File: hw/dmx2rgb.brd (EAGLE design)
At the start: 100 x 80 mm, 61 parts, among them IC1 ATMEGA88-20A, IC2 7805

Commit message: all parts added some parts placed
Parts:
- removed R10, R11, R12, R13, R9: 10k, dmx2rgb:CHIP_0805
- added C11, C12: 100n, dmx2rgb:CHIP_0805
- added LED1, LED2, LED3: (no value), dmx2rgb:CHIPLED_0805
- added PAD100, PAD17, PAD18, PAD19, PAD20, PAD21, PAD22, PAD23, PAD24, PAD25, PAD26, PAD27, PAD28, PAD29, PAD30, PAD31, PAD32, PAD33, PAD34, PAD35, PAD36, PAD37, PAD38, PAD39, PAD40, PAD41, PAD42, PAD43, PAD44, PAD45, PAD46, PAD47, PAD48, PAD49, PAD50, PAD51, PAD52, PAD53, PAD54, PAD55, PAD56, PAD57, PAD58, PAD59, PAD60, PAD61, PAD62, PAD63, PAD64, PAD65, PAD66, PAD67, PAD68, PAD69, PAD70, PAD71, PAD72, PAD73, PAD74, PAD75, PAD76, PAD77, PAD78, PAD79, PAD80, PAD81, PAD82, PAD83, PAD84, PAD85, PAD86, PAD87, PAD88, PAD89, PAD90, PAD91, PAD92, PAD93, PAD94, PAD95, PAD96, PAD99: (no value), dmx2rgb:SMD_PAD_LONG
- added PAD97, PAD98: (no value), dmx2rgb:SMD2,54-5,08
- added U$11, U$13, U$14, U$15, U$16, U$17, U$18, U$19, U$20, U$22, U$23, U$24, U$25, U$26, U$27, U$28: IRF7303, dmx2rgb:SO8
- added U$12, U$21: PCA9685, dmx2rgb:TSSOP28
- PAD1, PAD10, PAD11, PAD12, PAD13, PAD14, PAD15, PAD16, PAD2, PAD3, PAD4, PAD5, PAD6, PAD7, PAD8, PAD9: device dmx2rgb:PAD_THT_1.6 -> dmx2rgb:SMD_PAD_LONG
- R6, R7, R8: value 10k -> (none)
- moved SJ8 275.5 mm to (31.8, 77.5)
- moved SJ7 271.9 mm to (35.6, 77.5)
- moved SJ6 268.4 mm to (39.4, 77.5)
- moved SJ5 265.1 mm to (43.2, 77.5)
- moved SJ4 261.8 mm to (47.0, 77.5)
- moved SJ3 254.8 mm to (47.0, 74.9)
- moved SJ2 248.1 mm to (41.9, 74.9)
- moved SJ1 241.5 mm to (36.8, 74.9)
- moved R6 239.2 mm to (10.2, 43.2)
- moved R7 236.7 mm to (10.2, 38.1)
- moved R4 234.1 mm to (55.9, 64.8)
- moved R8 233.9 mm to (8.89, 33.0)
- moved C9 209.5 mm to (27.9, 69.8)
- moved C8 205.6 mm to (21.6, 72.4)
- moved C10 205.2 mm to (12.7, 63.5)
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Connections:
- removed net N$12: U$3.6
- removed net N$62: SJ5.1
- new net LED_ENABLE: IC1.1, R5.1, U$12.23, U$2.23, U$21.23
- new net N$100: PAD35.P$1, U$22.7, U$22.8
- new net N$101: PAD36.P$1, U$22.5, U$22.6
- new net N$102: U$21.10, U$22.4
- new net N$103: PAD37.P$1, U$23.7, U$23.8
- new net N$104: PAD38.P$1, U$23.5, U$23.6
- new net N$105: U$21.9, U$23.2
- new net N$106: U$21.8, U$23.4
- new net N$107: PAD39.P$1, U$24.7, U$24.8
- new net N$108: PAD40.P$1, U$24.5, U$24.6
- new net N$109: U$21.7, U$24.2
- new net N$110: U$21.6, U$24.4
- new net N$111: PAD41.P$1, U$25.7, U$25.8
- new net N$112: PAD42.P$1, U$25.5, U$25.6
- new net N$113: PAD43.P$1, U$26.7, U$26.8
- new net N$114: PAD44.P$1, U$26.5, U$26.6
- new net N$115: PAD45.P$1, U$27.7, U$27.8
- new net N$116: PAD46.P$1, U$27.5, U$27.6
- new net N$117: PAD47.P$1, U$28.7, U$28.8
- new net N$118: PAD48.P$1, U$28.5, U$28.6
- new net N$119: U$20.2, U$21.13
- new net N$120: U$20.4, U$21.12
- new net N$121: U$21.11, U$22.2
- new net N$122: U$21.15, U$25.2
- new net N$123: U$21.16, U$25.4
- new net N$124: U$21.17, U$26.2
- new net N$125: U$21.18, U$26.4
- new net N$126: U$21.19, U$27.2
- new net N$127: U$21.20, U$27.4
- new net N$128: U$21.21, U$28.2
- new net N$129: U$21.22, U$28.4
- new net N$47: PAD100.P$1, U$3.6
- new net N$48: PAD17.P$1, U$11.7, U$11.8
- new net N$49: PAD18.P$1, U$11.5, U$11.6
- new net N$61: PAD19.P$1, U$13.7, U$13.8
- new net N$63: PAD20.P$1, U$13.5, U$13.6
- new net N$64: U$12.10, U$13.4
- new net N$65: PAD21.P$1, U$14.7, U$14.8
- new net N$66: PAD22.P$1, U$14.5, U$14.6
- new net N$67: U$12.9, U$14.2
- new net N$68: U$12.8, U$14.4
- new net N$69: PAD23.P$1, U$15.7, U$15.8
- new net N$70: PAD24.P$1, U$15.5, U$15.6
- new net N$71: U$12.7, U$15.2
- new net N$72: U$12.6, U$15.4
- new net N$73: PAD25.P$1, U$16.7, U$16.8
- new net N$74: PAD26.P$1, U$16.5, U$16.6
- new net N$75: PAD27.P$1, U$17.7, U$17.8
- new net N$76: PAD28.P$1, U$17.5, U$17.6
- new net N$77: PAD29.P$1, U$18.7, U$18.8
- new net N$78: PAD30.P$1, U$18.5, U$18.6
- new net N$79: PAD31.P$1, U$19.7, U$19.8
- new net N$80: PAD32.P$1, U$19.5, U$19.6
- new net N$81: U$11.2, U$12.13
- new net N$82: U$11.4, U$12.12
- new net N$83: U$12.11, U$13.2
- new net N$84: U$12.15, U$16.2
- new net N$85: U$12.16, U$16.4
- new net N$86: U$12.17, U$17.2
- new net N$87: U$12.18, U$17.4
- new net N$88: U$12.19, U$18.2
- new net N$89: U$12.20, U$18.4
- new net N$90: U$12.21, U$19.2
- new net N$91: U$12.22, U$19.4
- new net N$98: PAD33.P$1, U$20.7, U$20.8
- new net N$99: PAD34.P$1, U$20.5, U$20.6
- net +12V: now also PAD49.P$1, PAD50.P$1, PAD51.P$1, PAD52.P$1, PAD53.P$1, PAD54.P$1, PAD55.P$1, PAD56.P$1, PAD57.P$1, PAD58.P$1, PAD59.P$1, PAD60.P$1, PAD61.P$1, PAD62.P$1, PAD63.P$1, PAD64.P$1, PAD65.P$1, PAD66.P$1, PAD67.P$1, PAD68.P$1, PAD69.P$1, PAD70.P$1, PAD71.P$1, PAD72.P$1, PAD73.P$1, PAD74.P$1, PAD75.P$1, PAD76.P$1, PAD77.P$1, PAD78.P$1, PAD79.P$1, PAD80.P$1, PAD81.P$1, PAD82.P$1, PAD83.P$1, PAD84.P$1, PAD85.P$1, PAD86.P$1, PAD87.P$1, PAD88.P$1, PAD89.P$1, PAD90.P$1, PAD91.P$1, PAD92.P$1, PAD93.P$1, PAD94.P$1, PAD95.P$1, PAD96.P$1, PAD97.1
- net +5V: now also C11.2, C12.2, LED1.A, LED2.A, LED3.A, U$12.1, U$12.2, U$12.28, U$2.1, U$21.1, U$21.2, U$21.28, U$21.3; no longer R10.2, R11.2, R12.2, R13.2, R6.2, R7.2, R8.2, R9.2
- net GND: now also C11.1, C12.1, PAD98.1, U$11.1, U$11.3, U$12.14, U$12.24, U$12.25, U$12.3, U$12.4, U$12.5, U$13.1, U$13.3, U$14.1, U$14.3, U$15.1, U$15.3, U$16.1, U$16.3, U$17.1, U$17.3, U$18.1, U$18.3, U$19.1, U$19.3, U$2.2, U$2.3, U$2.4, U$2.5, U$20.1, U$20.3, U$21.14, U$21.24, U$21.25, U$21.4, U$21.5, U$22.1, U$22.3, U$23.1, U$23.3, U$24.1, U$24.3, U$25.1, U$25.3, U$26.1, U$26.3, U$27.1, U$27.3, U$28.1, U$28.3
- net N$11: now also PAD99.P$1
- net N$15: now also LED2.C, R7.2; no longer U$2.1
- net N$27: now also LED1.C, R6.2; no longer U$2.2
- net N$28: now also IC1.12, R6.1; no longer U$2.3
- net N$3: now also LED3.C, R8.2; no longer IC1.32, R5.1, U$3.2
- net N$31: now also IC1.13, R7.1; no longer U$2.4
- net N$32: now also IC1.14, R8.1; no longer U$2.5
- net N$35: no longer R6.1
- net N$36: no longer R7.1
- net N$39: no longer R8.1
- net N$4: now also IC1.32, U$3.2; no longer IC1.1
- net N$40: no longer R9.1
- net N$43: now also IC1.2, SJ5.1; no longer IC1.11, R13.1
- net N$44: now also IC1.9; no longer IC1.12, R12.1
- net N$45: now also IC1.10; no longer IC1.13, R11.1
- net N$46: now also IC1.11; no longer IC1.14, R10.1
- net SCL: now also U$12.26, U$21.26
- net SDA: now also U$12.27, U$21.27

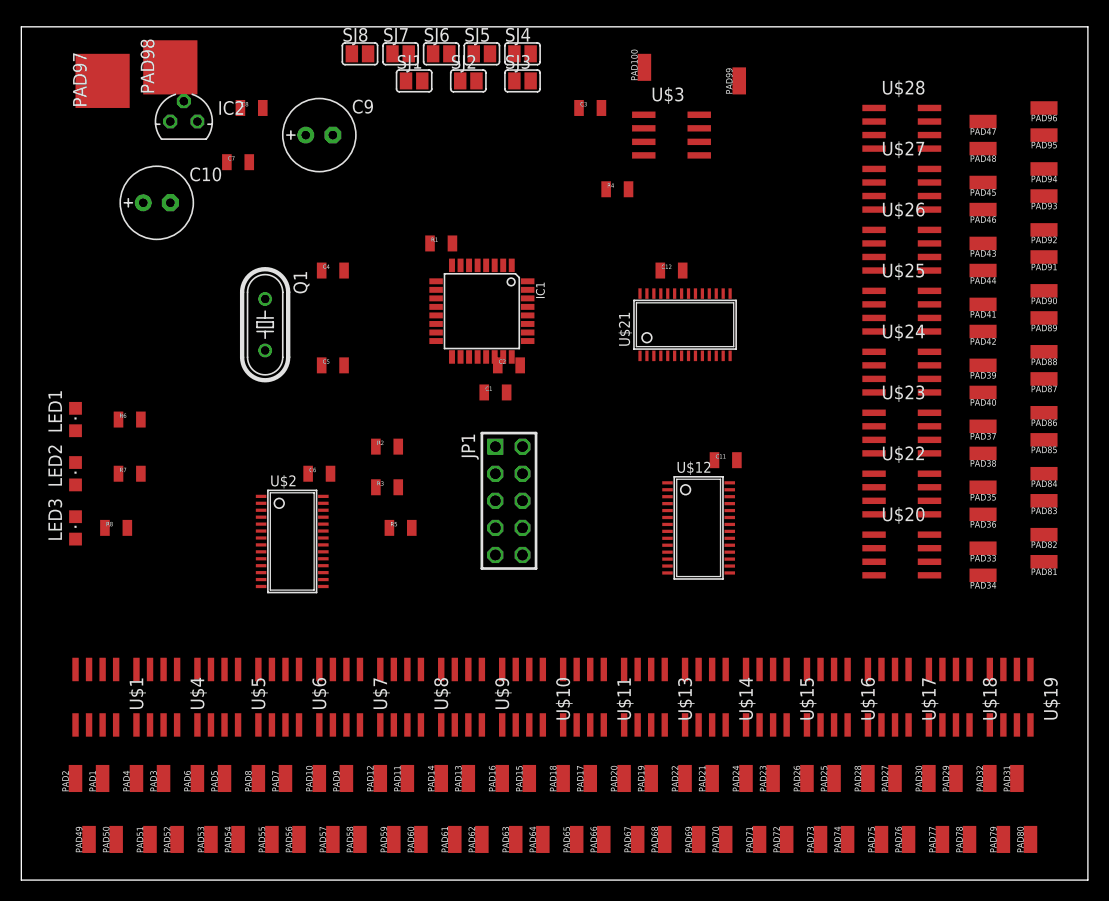
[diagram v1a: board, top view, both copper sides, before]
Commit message: pcb finished prepared for 0.3mm milling
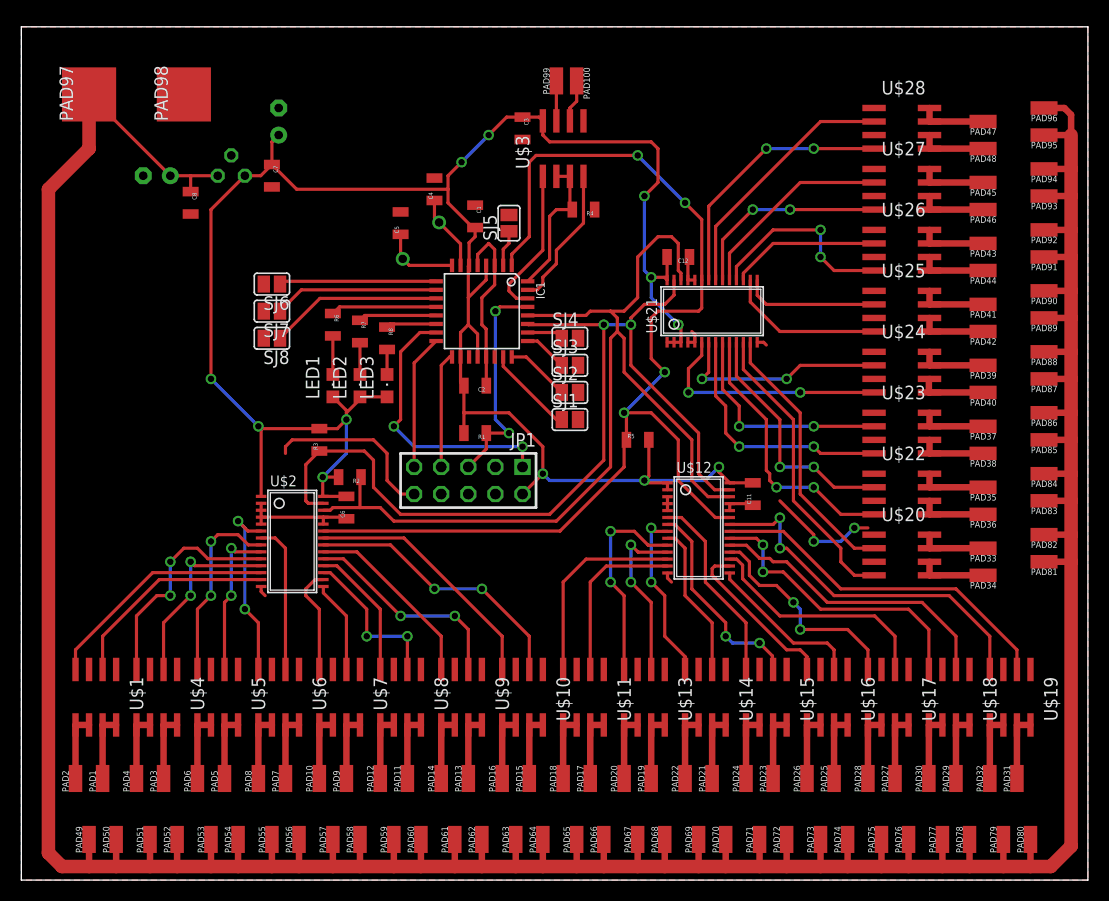
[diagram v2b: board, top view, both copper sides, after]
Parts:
- moved SJ1 34.9 mm to (51.4, 43.2)
- moved LED3 32.1 mm to (34.3, 46.4)
- moved R8 31.0 mm to (34.3, 50.8), turned to 270 degrees
- moved SJ2 30.7 mm to (51.4, 45.7)
- moved LED2 27.9 mm to (31.8, 46.4)
- moved SJ8 27.9 mm to (23.5, 50.8), turned to 180 degrees
- moved SJ3 27.0 mm to (51.4, 48.3)
- moved SJ4 27.0 mm to (51.4, 50.8)
- moved SJ7 27.0 mm to (23.5, 53.3), turned to 180 degrees
- moved SJ6 26.8 mm to (23.5, 55.9), turned to 180 degrees
- moved R7 25.4 mm to (31.8, 51.4), turned to 270 degrees
- moved LED1 24.3 mm to (29.2, 46.4)
- moved R5 23.7 mm to (57.8, 41.3)
- moved R6 21.0 mm to (29.2, 52.1), turned to 270 degrees
- moved R1 18.1 mm to (42.5, 41.9), turned to 180 degrees
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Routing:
- net +12V: track 0.00 -> 377.4 mm
- net +5V: track 0.00 -> 209.4 mm, vias 0 -> 12
- net LED_ENABLE: track 0.00 -> 105.9 mm, vias 0 -> 4
- net SCL: track 0.00 -> 91.9 mm
- net SDA: track 0.00 -> 89.7 mm, vias 0 -> 2
- net GND: track 0.00 -> 66.5 mm, vias 0 -> 2
- net N$91: track 0.00 -> 34.0 mm, vias 0 -> 2
- net N$90: track 0.00 -> 33.4 mm
- net N$120: track 0.00 -> 28.0 mm
- net N$88: track 0.00 -> 27.9 mm
- net N$89: track 0.00 -> 27.5 mm, vias 0 -> 2
- net N$8: track 0.00 -> 26.1 mm, vias 0 -> 2
- net N$59: track 0.00 -> 26.0 mm, vias 0 -> 2
- net N$102: track 0.00 -> 25.6 mm, vias 0 -> 2
- net N$119: track 0.00 -> 25.2 mm
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- added copper zone on layer 1, net GND

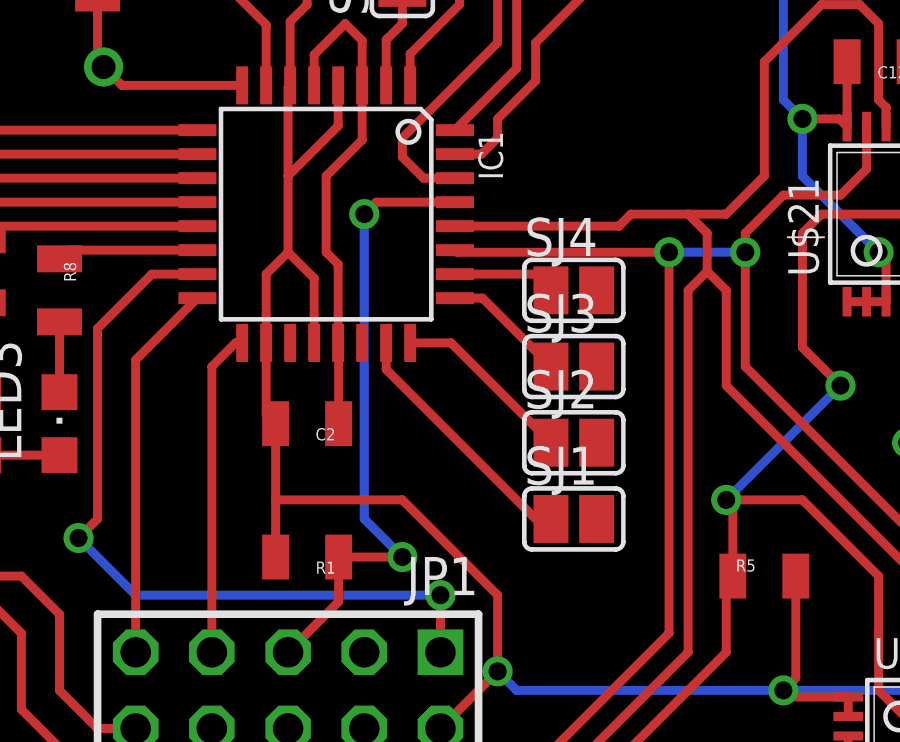
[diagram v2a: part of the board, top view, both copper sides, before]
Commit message: removed drilling below mcu
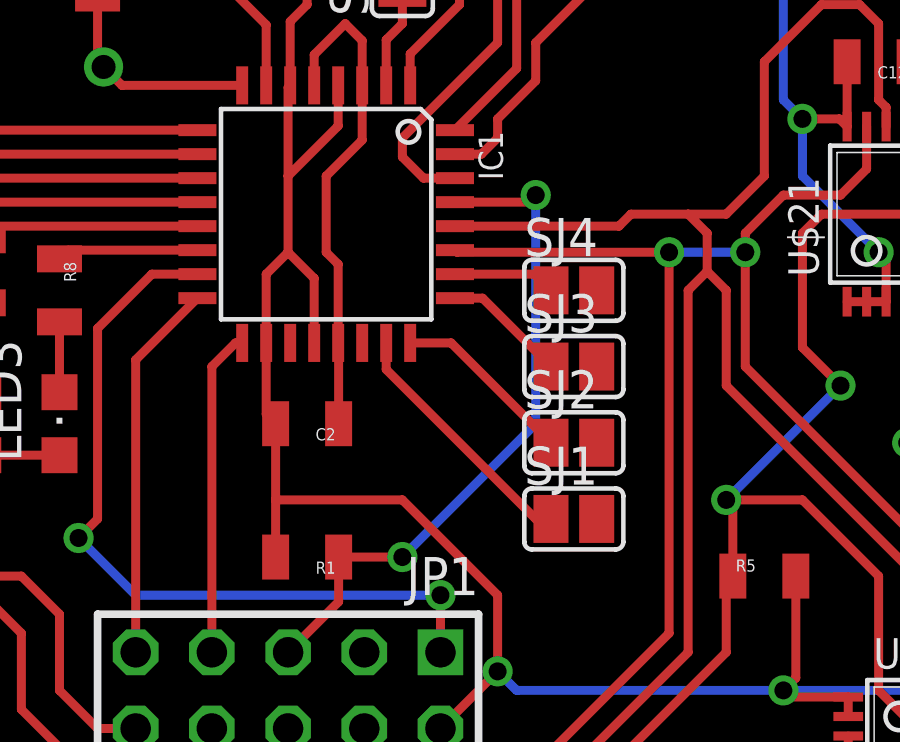
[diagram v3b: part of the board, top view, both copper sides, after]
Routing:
- net N$7: track 21.1 -> 22.7 mm
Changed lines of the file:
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@@
 <wire x1="41.91" y1="38.735" x2="43.595" y2="40.42" width="0.3" layer="1"/>
 <via x="45.72" y="41.91" extent="1-16" drill="0.6"/>
-<wire x1="44.45" y1="43.18" x2="44.45" y2="53.34" width="0.3" layer="16"/>
-<via x="44.45" y="53.34" extent="1-16" drill="0.6"/>
-<wire x1="44.45" y1="53.34" x2="44.85" y2="53.74" width="0.3" layer="1"/>
-<wire x1="44.85" y1="53.74" x2="47.4726" y2="53.74" width="0.3" layer="1"/>
+<via x="50.165" y="53.975" extent="1-16" drill="0.6"/>
 <wire x1="43.595" y1="40.42" x2="43.595" y2="41.91" width="0.3" layer="1"/>
-<wire x1="44.45" y1="43.18" x2="45.72" y2="41.91" width="0.3" layer="16"/>
 <wire x1="45.72" y1="41.91" x2="43.595" y2="41.91" width="0.3" layer="1"/>
+<wire x1="45.72" y1="41.91" x2="50.165" y2="46.355" width="0.3" layer="16"/>
+<wire x1="50.165" y1="46.355" x2="50.165" y2="53.975" width="0.3" layer="16"/>
+<wire x1="50.165" y1="53.975" x2="49.93" y2="53.74" width="0.3" layer="1"/>
+<wire x1="49.93" y1="53.74" x2="47.4726" y2="53.74" width="0.3" layer="1"/>
 </signal>
 <signal name="N$8">

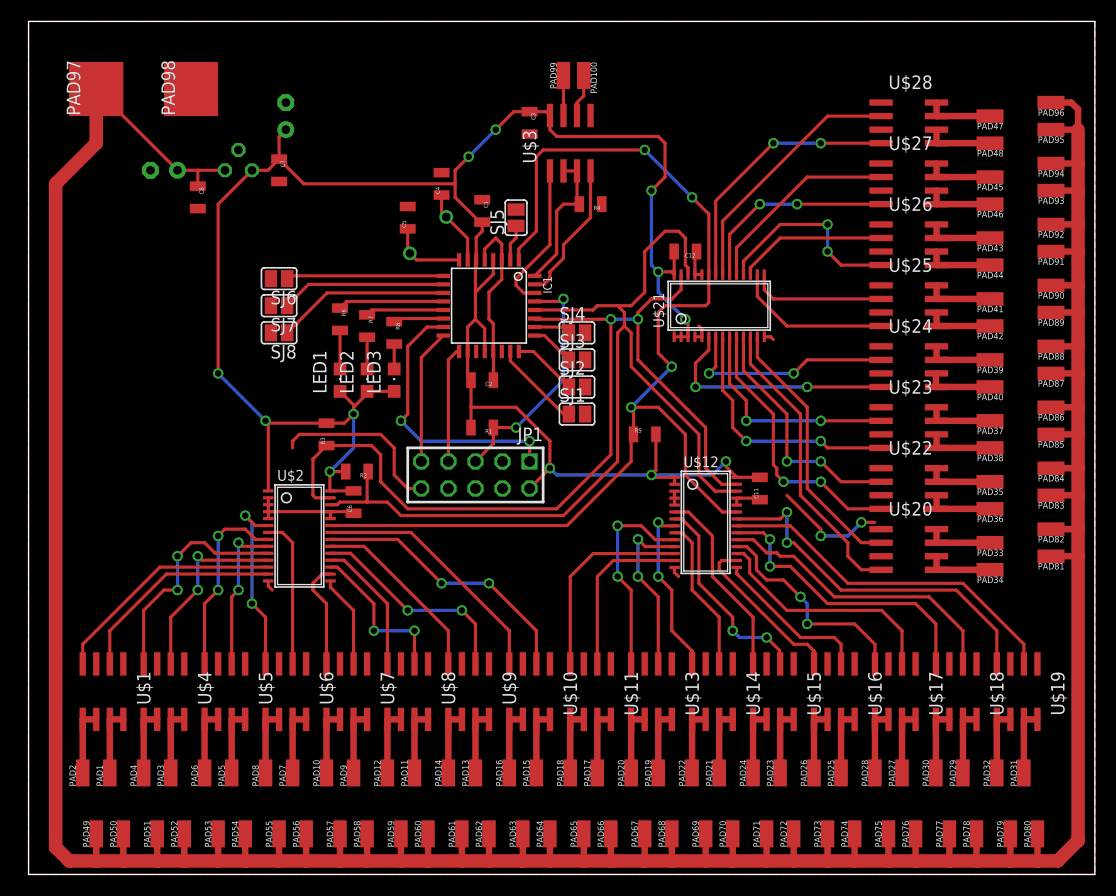
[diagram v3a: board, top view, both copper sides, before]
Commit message: optimized and doublesided
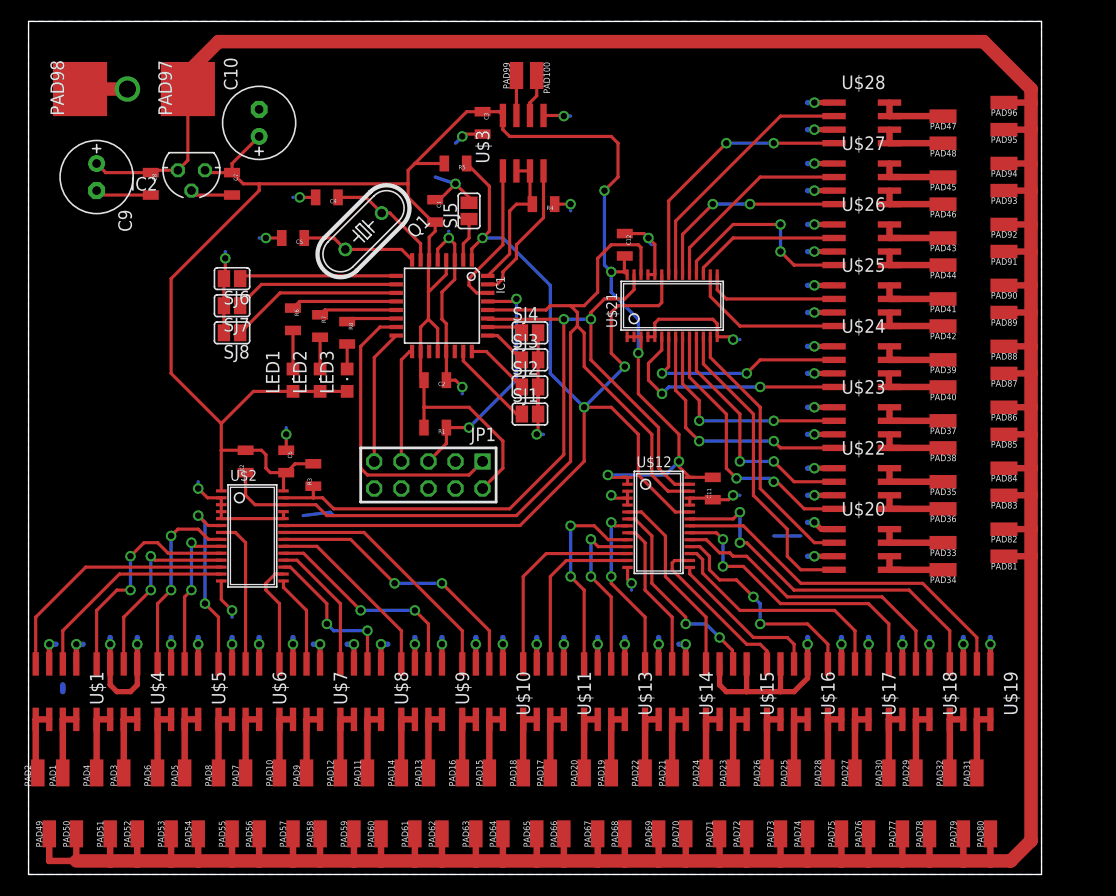
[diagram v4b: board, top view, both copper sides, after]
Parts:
- moved R5 31.0 mm to (40.0, 66.7), turned to 180 degrees
- moved C5 10.9 mm to (24.8, 59.7), turned to 180 degrees
- moved C4 10.8 mm to (28.0, 63.5), turned to 180 degrees
- moved R2 10.5 mm to (20.4, 38.7), turned to 90 degrees
- moved PAD98 10.4 mm to (4.83, 73.7)
- moved PAD97 8.59 mm to (14.9, 73.7)
- moved C6 7.38 mm to (24.2, 38.7), turned to 270 degrees
- moved C9 6.35 mm to (6.38, 65.4), flipped to the top, turned to 270 degrees
- moved Q1 6.06 mm to (31.4, 60.3), flipped to the top, turned to 225 degrees
- moved C12 5.72 mm to (55.9, 59.1), turned to 270 degrees
- moved C7 4.59 mm to (19.1, 64.8)
- moved C8 4.59 mm to (11.5, 64.8)
- moved SJ5 4.46 mm to (41.3, 62.2)
- moved PAD27 4.41 mm to (77.5, 9.53)
- moved PAD32 4.41 mm to (86.4, 9.53)
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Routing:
- net GND: track 66.5 -> 262.5 mm, vias 2 -> 64
- net SDA: track 89.7 -> 79.4 mm
- net +12V: track 377.4 -> 385.0 mm
- net N$41: track 7.10 -> 11.1 mm
- net N$42: track 7.26 -> 11.0 mm
- net LED_ENABLE: track 105.9 -> 102.6 mm, vias 4 -> 3
- net N$8: track 26.1 -> 27.7 mm, vias 2 -> 0
- net +5V: track 209.4 -> 211.0 mm, vias 12 -> 5
- net N$51: track 22.2 -> 23.7 mm
- net SCL: track 91.9 -> 93.1 mm
- net N$120: track 28.0 -> 28.7 mm
- net N$43: track 3.42 -> 4.06 mm
- added copper zone on layer 16, net GND
- removed copper zone on layer 1, net GND
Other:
- board size 100 x 80 mm -> 95 x 80 mm
